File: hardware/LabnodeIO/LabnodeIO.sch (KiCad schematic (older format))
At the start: 17 parts, among them J1 mc 0.5-2.5, J2 EXT3, J3 mc 0.5-2.5, U1 PCF8574, U2 LM324

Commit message: layout labnodeIO
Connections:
- net +12V: now also J1.1 (Pin_1), J1.2 (Pin_2); no longer J1.9 (Pin_9)
- net at U1.10 (P5): now also J1.5 (Pin_5); no longer J1.6 (Pin_6)
- net at U1.11 (P6): now also J1.4 (Pin_4); no longer J1.7 (Pin_7)
- net at U1.12 (P7): now also J1.3 (Pin_3); no longer J1.8 (Pin_8)
- net at U1.4 (P0): now also J1.10 (Pin_10); no longer J1.1 (Pin_1)
- net at U1.5 (P1): now also J1.9 (Pin_9); no longer J1.2 (Pin_2)
- net at U1.6 (P2): now also J1.8 (Pin_8); no longer J1.3 (Pin_3)
- net at U1.7 (P3): now also J1.7 (Pin_7); no longer J1.4 (Pin_4)
- net at U1.9 (P4): now also J1.6 (Pin_6); no longer J1.5 (Pin_5)
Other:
- moved on the sheet: J1
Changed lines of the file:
@@
 LIBS:contrib
 LIBS:valves
+LIBS:LabnodeIO-cache
 EELAYER 25 0
 EELAYER END
@@
 L Conn_01x10 J1
 U 1 1 5A8D8458
-P 5200 2400
-F 0 "J1" H 5200 2900 50  0000 C CNN
-F 1 "mc 0.5-2.5" V 5350 2050 50  0000 C CNN
-F 2 "Connectors_Molex:Molex_KK-6410-10_10x2.54mm_Straight" H 5200 2400 50  0001 C CNN
-F 3 "" H 5200 2400 50  0001 C CNN
-	1    5200 2400
-	1    0    0    -1
-$EndComp
-Wire Wire Line
-	5000 2000 4700 2000
-Wire Wire Line
-	4700 2100 5000 2100
-Wire Wire Line
-	5000 2200 4700 2200
-Wire Wire Line
-	4700 2300 5000 2300
-Wire Wire Line
-	5000 2400 4700 2400
-Wire Wire Line
-	4700 2500 5000 2500
-Wire Wire Line
-	4700 2600 5000 2600
-Wire Wire Line
-	5000 2700 4700 2700
+P 5450 2500
+F 0 "J1" H 5450 3000 50  0000 C CNN
+F 1 "mc 0.5-2.5" V 5600 2150 50  0000 C CNN
+F 2 "Connectors_Molex:Molex_KK-6410-10_10x2.54mm_Straight" H 5450 2500 50  0001 C CNN
+F 3 "" H 5450 2500 50  0001 C CNN
+	1    5450 2500
+	1    0    0    1
+$EndComp
+Wire Wire Line
+	5250 2000 4700 2000
+Wire Wire Line
+	4700 2100 5250 2100
+Wire Wire Line
+	5250 2200 4700 2200
+Wire Wire Line
+	4700 2300 5250 2300
+Wire Wire Line
+	5250 2400 4700 2400
+Wire Wire Line
+	4700 2500 5250 2500
+Wire Wire Line
+	4700 2600 5250 2600
+Wire Wire Line
+	5250 2700 4700 2700
 $Comp
 L +12V #PWR05
@@
 $EndComp
 Wire Wire Line
-	4850 2800 5000 2800
+	4850 2800 5250 2800
 $Comp
 L LM324 U2
@@
 	3750 4500 3750 4250
 Connection ~ 3750 4250
+Wire Wire Line
+	5250 2900 5150 2900
+Wire Wire Line
+	5150 2900 5150 2800
+Connection ~ 5150 2800
 $EndSCHEMATC

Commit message: layout fertig
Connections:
- wire segments 72 -> 76
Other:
- moved on the sheet: J1
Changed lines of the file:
@@
 L Conn_01x10 J1
 U 1 1 5A8D8458
-P 5450 2500
-F 0 "J1" H 5450 3000 50  0000 C CNN
-F 1 "mc 0.5-2.5" V 5600 2150 50  0000 C CNN
-F 2 "Connectors_Molex:Molex_KK-6410-10_10x2.54mm_Straight" H 5450 2500 50  0001 C CNN
-F 3 "" H 5450 2500 50  0001 C CNN
-	1    5450 2500
+P 5450 2300
+F 0 "J1" H 5450 2800 50  0000 C CNN
+F 1 "mc 0.5-2.5" V 5600 1950 50  0000 C CNN
+F 2 "Connectors_Molex:Molex_KK-6410-10_10x2.54mm_Straight" H 5450 2300 50  0001 C CNN
+F 3 "" H 5450 2300 50  0001 C CNN
+	1    5450 2300
 	1    0    0    1
 $EndComp
@@
 L +12V #PWR05
 U 1 1 5A8D8554
-P 4850 2800
-F 0 "#PWR05" H 4850 2650 50  0001 C CNN
-F 1 "+12V" V 4750 2900 50  0000 C CNN
-F 2 "" H 4850 2800 50  0001 C CNN
-F 3 "" H 4850 2800 50  0001 C CNN
-	1    4850 2800
+P 5000 1800
+F 0 "#PWR05" H 5000 1650 50  0001 C CNN
+F 1 "+12V" V 4900 1900 50  0000 C CNN
+F 2 "" H 5000 1800 50  0001 C CNN
+F 3 "" H 5000 1800 50  0001 C CNN
+	1    5000 1800
 	0    -1   -1   0
 $EndComp
@@
 	5150 2900 5150 2800
 Connection ~ 5150 2800
+Wire Wire Line
+	5000 1800 5250 1800
+Wire Wire Line
+	5250 1900 5100 1900
+Wire Wire Line
+	5100 1900 5100 1800
+Connection ~ 5100 1800
+$Comp
+L +12V #PWR019
+U 1 1 5A8EB4AA
+P 2650 2550
+F 0 "#PWR019" H 2650 2400 50  0001 C CNN
+F 1 "+12V" H 2650 2690 50  0000 C CNN
+F 2 "" H 2650 2550 50  0001 C CNN
+F 3 "" H 2650 2550 50  0001 C CNN
+	1    2650 2550
+	0    1    1    0
+$EndComp
+Wire Wire Line
+	2650 2550 2400 2550
 $EndSCHEMATC

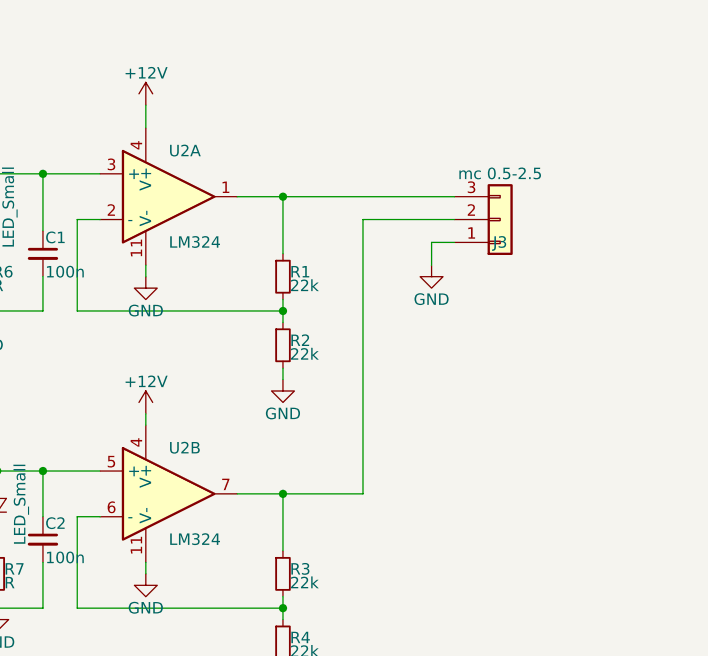
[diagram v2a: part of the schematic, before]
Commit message: Ausgangskondensatoren eingefügt
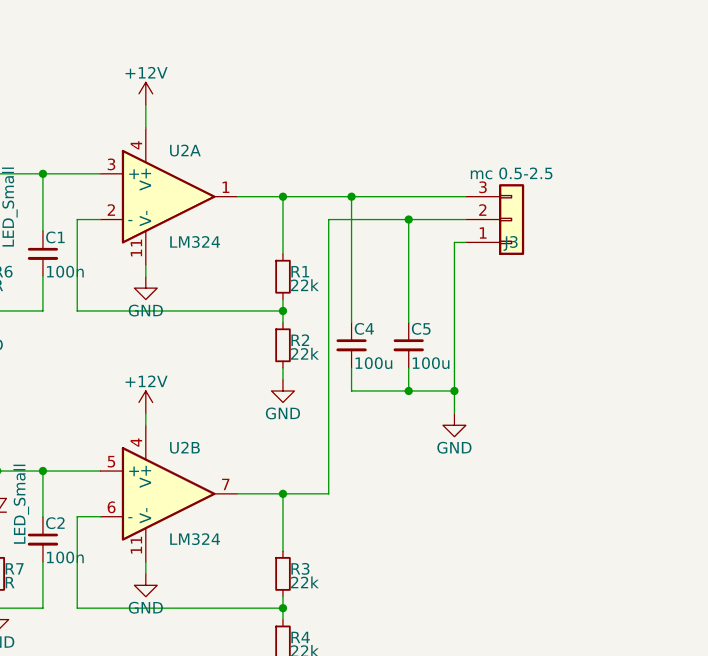
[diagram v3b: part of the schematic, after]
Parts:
- added C4, C5: 100u, Capacitors_THT:CP_Radial_D4.0mm_P2.00mm, symbol C_Small
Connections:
- wire segments 76 -> 81
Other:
- moved on the sheet: J3
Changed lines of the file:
@@
 	4800 4600 4800 4350
 Wire Wire Line
-	4600 4350 5550 4350
+	4600 4350 5600 4350
 Wire Wire Line
 	4000 4450 3900 4450
@@
 L Conn_01x03 J3
 U 1 1 5A8DA5A8
-P 5750 4450
-F 0 "J3" H 5750 4550 50  0000 C CNN
-F 1 "mc 0.5-2.5" H 5750 4250 50  0000 C CNN
-F 2 "Connectors_Molex:Molex_KK-6410-03_03x2.54mm_Straight" H 5750 4450 50  0001 C CNN
-F 3 "" H 5750 4450 50  0001 C CNN
-	1    5750 4450
+P 5800 4450
+F 0 "J3" H 5800 4550 50  0000 C CNN
+F 1 "mc 0.5-2.5" H 5800 4250 50  0000 C CNN
+F 2 "Connectors_Molex:Molex_KK-6410-03_03x2.54mm_Straight" H 5800 4450 50  0001 C CNN
+F 3 "" H 5800 4450 50  0001 C CNN
+	1    5800 4450
 	1    0    0    1
 $EndComp
@@
 L GND #PWR016
 U 1 1 5A8DAB0F
-P 5450 4650
-F 0 "#PWR016" H 5450 4400 50  0001 C CNN
-F 1 "GND" H 5450 4500 50  0000 C CNN
-F 2 "" H 5450 4650 50  0001 C CNN
-F 3 "" H 5450 4650 50  0001 C CNN
-	1    5450 4650
-	1    0    0    -1
-$EndComp
-Wire Wire Line
-	5450 4650 5450 4550
-Wire Wire Line
-	5450 4550 5550 4550
-Wire Wire Line
-	5550 4450 5150 4450
-Wire Wire Line
-	5150 4450 5150 5650
-Wire Wire Line
-	5150 5650 4600 5650
+P 5550 5300
+F 0 "#PWR016" H 5550 5050 50  0001 C CNN
+F 1 "GND" H 5550 5150 50  0000 C CNN
+F 2 "" H 5550 5300 50  0001 C CNN
+F 3 "" H 5550 5300 50  0001 C CNN
+	1    5550 5300
+	1    0    0    -1
+$EndComp
+Wire Wire Line
+	5550 5300 5550 4550
+Wire Wire Line
+	5550 4550 5600 4550
+Wire Wire Line
+	5600 4450 5000 4450
+Wire Wire Line
+	5000 4450 5000 5650
+Wire Wire Line
+	5000 5650 4600 5650
 $Comp
 L C_Small C3
@@
 Wire Wire Line
 	2650 2550 2400 2550
+$Comp
+L C_Small C5
+U 1 1 5A8EE115
+P 5350 5000
+F 0 "C5" H 5360 5070 50  0000 L CNN
+F 1 "100u" H 5360 4920 50  0000 L CNN
+F 2 "Capacitors_THT:CP_Radial_D4.0mm_P2.00mm" H 5350 5000 50  0001 C CNN
+F 3 "" H 5350 5000 50  0001 C CNN
+	1    5350 5000
+	1    0    0    -1
+$EndComp
+$Comp
+L C_Small C4
+U 1 1 5A8EE2AB
+P 5100 5000
+F 0 "C4" H 5110 5070 50  0000 L CNN
+F 1 "100u" H 5110 4920 50  0000 L CNN
+F 2 "Capacitors_THT:CP_Radial_D4.0mm_P2.00mm" H 5100 5000 50  0001 C CNN
+F 3 "" H 5100 5000 50  0001 C CNN
+	1    5100 5000
+	1    0    0    -1
+$EndComp
+Wire Wire Line
+	5100 4900 5100 4350
+Connection ~ 5100 4350
+Wire Wire Line
+	5350 4900 5350 4450
+Connection ~ 5350 4450
+Wire Wire Line
+	5350 5100 5350 5200
+Wire Wire Line
+	5100 5200 5550 5200
+Connection ~ 5550 5200
+Wire Wire Line
+	5100 5200 5100 5100
+Connection ~ 5350 5200
 $EndSCHEMATC

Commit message: 5v auf stecker
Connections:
- wire segments 81 -> 83
- no-connect marks 0 -> 1
